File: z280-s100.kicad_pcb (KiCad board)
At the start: 4 copper layers, 254 x 134.6 mm, 58 parts, among them J10 Config (3x8), J7 Serial (2x5), J8 S-100 edge, J9 JTAG (1x6), U1 Z280 (PLCC-68), U10 28C256 even, U11 28C256 odd, U12 7805, U13 DS1813 reset, U14 MAX232, U15 74HCT245 addr0, U16 74HCT245 addr1, U17 74HCT245 addr2, U18 74HCT245 status, U19 74HCT245 control, U2 74HC573 latch, U20 74HCT245 pHLDA, U21 74HCT244 BTI, U22 74F138 decode, U23 74F521 flash win, U24 74F521 slave win, U25 74F245 DO, U26 74F245 DI, U3 74HC573 latch, U4 ATF1508 control, U5 ATF1508 data, U6 SRAM bank0 even, U7 SRAM bank0 odd, U8 SRAM bank1 even, U9 SRAM bank1 odd, Y1 24 MHz crystal

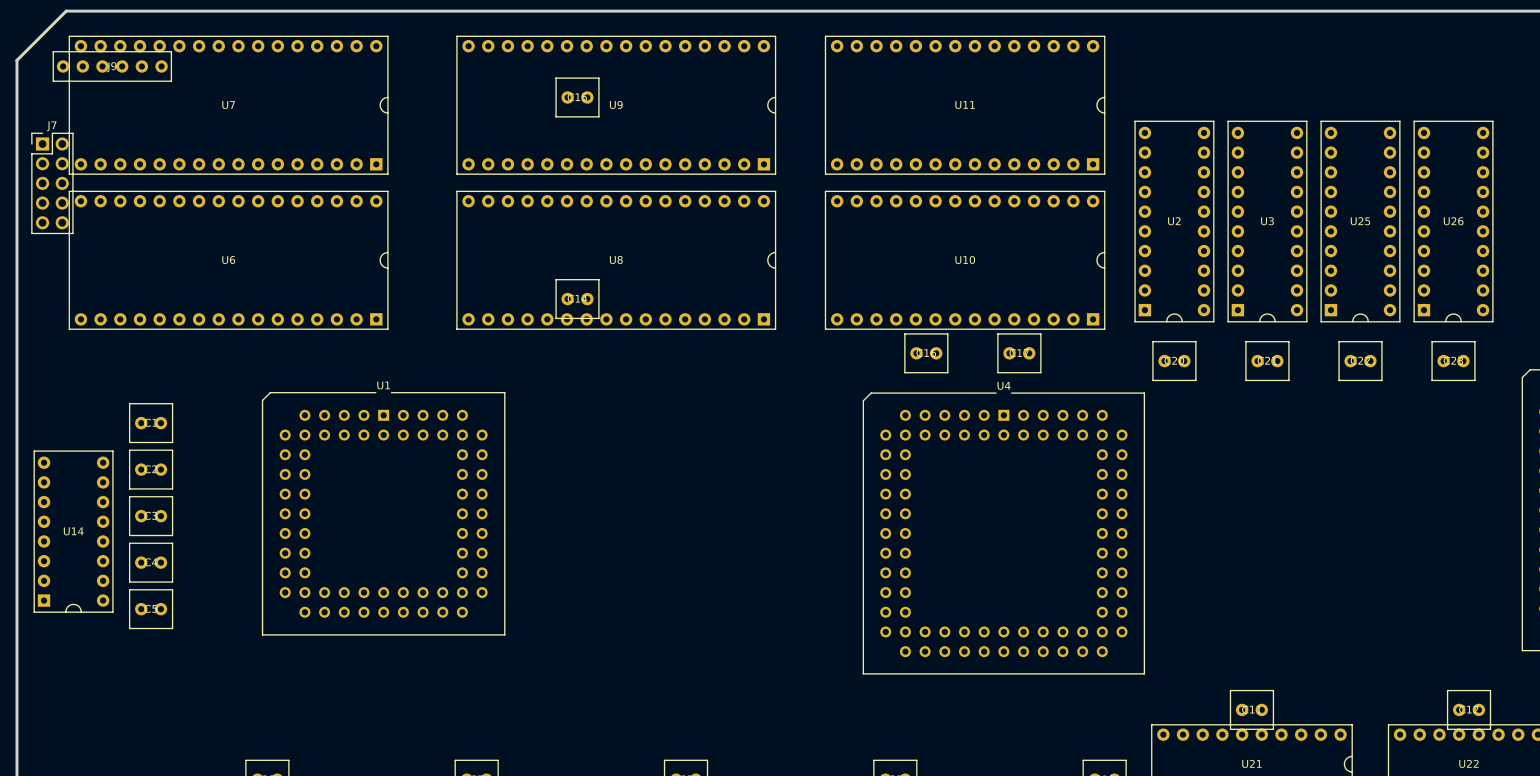
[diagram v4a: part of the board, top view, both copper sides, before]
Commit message: Z280 S-100: fix schematic annotations; rework schematic + PCB placement
The schematic was showing every reference as anonymous (U?, Y?) in KiCad.
Root cause: the symbol instances-block `path` was a filesystem path instead
of the root-sheet UUID, so KiCad couldn't resolve per-instance references.
Also `fields_autoplaced` was "no" (KiCad 9 wants "yes") and the
`sheet_instances` block was missing. Fixed all three.

Schematic placement: console (MAX232 + serial header) moved to the S-100
connector column; U25/U26 data-bus buffers given vertical spacing; U3 moved
down; J10 config and U21 BTI driver moved to the CPU column (x=88).

PCB placement: MAX232 + serial moved under the S-100 connector; data-bus
buffers stacked vertically; address-latch 74HC573s and bypass caps shifted to
match. DRC remains clean (no electrical shorts).

Co-Authored-By: Claude Code <noreply@anthropic.com>
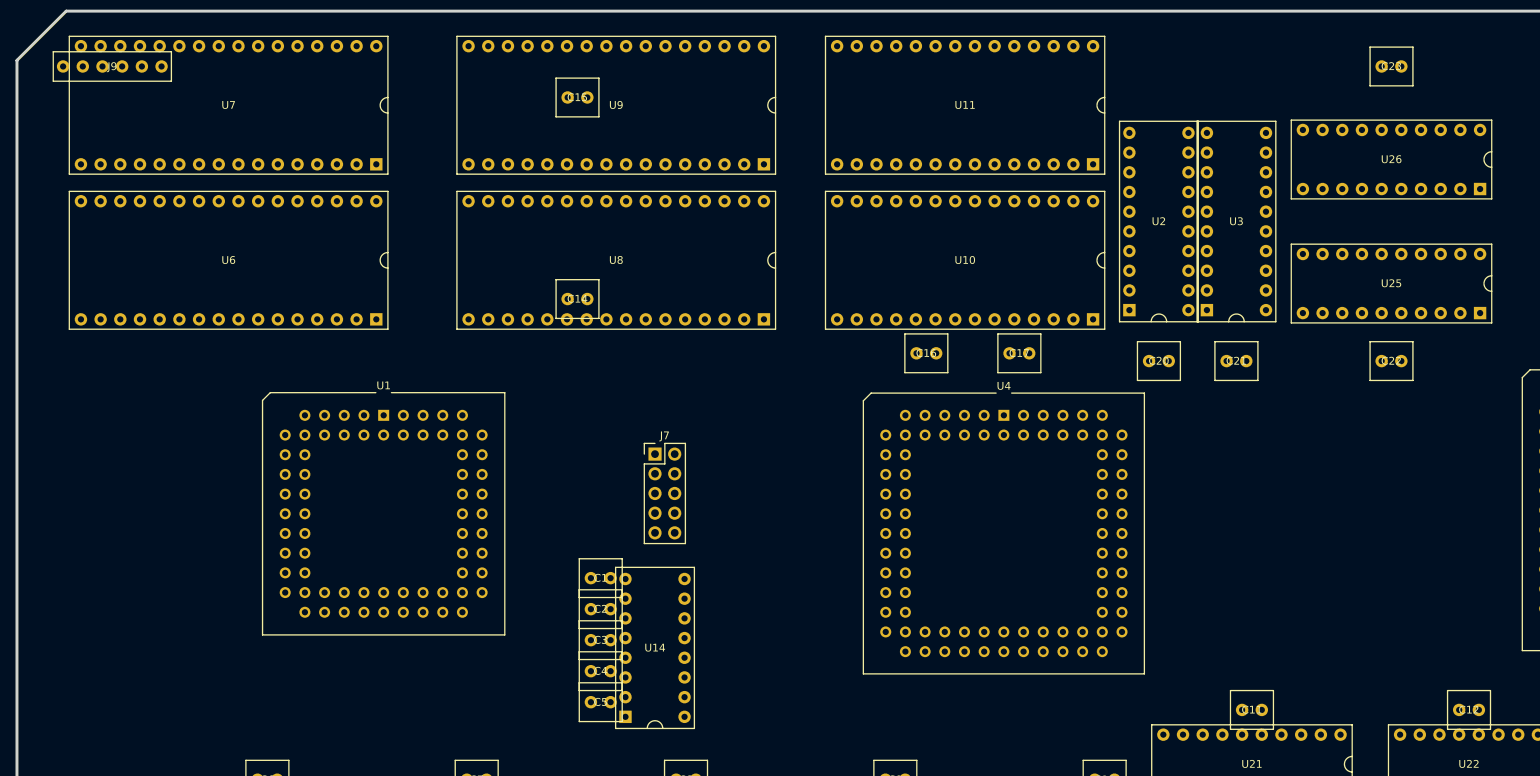
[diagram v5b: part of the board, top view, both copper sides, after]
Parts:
- moved J7 88.5 mm to (95.0, 80.0)
- moved U14 76.5 mm to (95.0, 105.0)
- moved C1 61.4 mm to (88.0, 96.0)
- moved C2 60.7 mm to (88.0, 100.0)
- moved C3 60.2 mm to (88.0, 104.0)
- moved C4 59.7 mm to (88.0, 108.0)
- moved C5 59.2 mm to (88.0, 112.0)
- moved C23 38.8 mm to (190.0, 30.0)
- moved U26 11.3 mm to (190.0, 42.0), turned to 90 degrees
- moved U25 8.94 mm to (190.0, 58.0), turned to 90 degrees
- moved C21 4.00 mm to (170.0, 68.0)
- moved C22 4.00 mm to (190.0, 68.0)
- moved U3 4.00 mm to (170.0, 50.0)
- moved C20 2.00 mm to (160.0, 68.0)
- moved U2 2.00 mm to (160.0, 50.0)
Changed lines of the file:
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@@
   )
   (footprint "DIP-20" (layer "F.Cu")
-    (at 186.0000 50.0000 0)
+    (at 190.0000 58.0000 90)
     (property "Reference" "U25" (at 0 0 0) (layer "F.SilkS")
       (effects (font (size 1 1))))
@@
   )
   (footprint "DIP-20" (layer "F.Cu")
-    (at 198.0000 50.0000 0)
+    (at 190.0000 42.0000 90)
     (property "Reference" "U26" (at 0 0 0) (layer "F.SilkS")
       (effects (font (size 1 1))))
@@
   )
   (footprint "DIP-20" (layer "F.Cu")
-    (at 162.0000 50.0000 0)
+    (at 160.0000 50.0000 0)
     (property "Reference" "U2" (at 0 0 0) (layer "F.SilkS")
       (effects (font (size 1 1))))
@@
   )
   (footprint "DIP-20" (layer "F.Cu")
-    (at 174.0000 50.0000 0)
+    (at 170.0000 50.0000 0)
     (property "Reference" "U3" (at 0 0 0) (layer "F.SilkS")
       (effects (font (size 1 1))))
@@
   )
   (footprint "DIP-16" (layer "F.Cu")
-    (at 20.0000 90.0000 0)
+    (at 95.0000 105.0000 0)
     (property "Reference" "U14" (at 0 0 0) (layer "F.SilkS")
       (effects (font (size 1 1))))
@@
 (footprint "Connector_PinHeader_2.54mm:PinHeader_2x05_P2.54mm_Vertical"
 	(layer "F.Cu")
-  (at 16.0000 40.0000 0)
+  (at 95.0000 80.0000 0)
 	(property "Reference" "J7"
 		(at 1.27 -2.38 0)
@@
   )
   (footprint "CAP-2" (layer "F.Cu")
-    (at 30.0000 76.0000 0)
+    (at 88.0000 96.0000 0)
     (property "Reference" "C1" (at 0 0 0) (layer "F.SilkS")
       (effects (font (size 1 1))))
@@
   )
   (footprint "CAP-2" (layer "F.Cu")
-    (at 30.0000 82.0000 0)
+    (at 88.0000 100.0000 0)
     (property "Reference" "C2" (at 0 0 0) (layer "F.SilkS")
       (effects (font (size 1 1))))
@@
   )
   (footprint "CAP-2" (layer "F.Cu")
-    (at 30.0000 88.0000 0)
+    (at 88.0000 104.0000 0)
     (property "Reference" "C3" (at 0 0 0) (layer "F.SilkS")
       (effects (font (size 1 1))))
@@
   )
   (footprint "CAP-2" (layer "F.Cu")
-    (at 30.0000 94.0000 0)
+    (at 88.0000 108.0000 0)
     (property "Reference" "C4" (at 0 0 0) (layer "F.SilkS")
       (effects (font (size 1 1))))
@@
   )
   (footprint "CAP-2" (layer "F.Cu")
-    (at 30.0000 100.0000 0)
+    (at 88.0000 112.0000 0)
     (property "Reference" "C5" (at 0 0 0) (layer "F.SilkS")
       (effects (font (size 1 1))))
@@
   )
   (footprint "CAP-2" (layer "F.Cu")
-    (at 162.0000 68.0000 0)
+    (at 160.0000 68.0000 0)
     (property "Reference" "C20" (at 0 0 0) (layer "F.SilkS")
       (effects (font (size 1 1))))
@@
   )
   (footprint "CAP-2" (layer "F.Cu")
-    (at 174.0000 68.0000 0)
+    (at 170.0000 68.0000 0)
     (property "Reference" "C21" (at 0 0 0) (layer "F.SilkS")
       (effects (font (size 1 1))))
@@
   )
   (footprint "CAP-2" (layer "F.Cu")
-    (at 186.0000 68.0000 0)
+    (at 190.0000 68.0000 0)
     (property "Reference" "C22" (at 0 0 0) (layer "F.SilkS")
       (effects (font (size 1 1))))
@@
   )
   (footprint "CAP-2" (layer "F.Cu")
-    (at 198.0000 68.0000 0)
+    (at 190.0000 30.0000 0)
     (property "Reference" "C23" (at 0 0 0) (layer "F.SilkS")
       (effects (font (size 1 1))))

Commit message: Z280 S-100: deterministic schematic UUIDs; unify S-100 footprint name
uid() now derives each schematic UUID from a stable identity key (uuid5) instead of uuid4, so regenerating the schematic no longer churns symbol UUIDs; the board's footprint (path ...) links survive Update PCB from Schematic.

S-100 edge connector footprint unified on S100_MALE (the schematic carried a phantom Connector_Edge that broke net updates). Sync U27/Y2/U13/J7 positions from the schematic; regenerate the netlist and update the board's 42 footprint path UUIDs to match.

Also rename decode signal BANK -> A20 and convert DIP/header placements to library footprints in gen_pcb.py.

Co-Authored-By: Claude Code <noreply@anthropic.com>
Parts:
- added U27: LM323K, Package_TO_SOT_THT:TO-3, F.Cu at (50.5, 123.2)
- added Y2: 24 MHz, z280-s100:Oscillator_DIP-8-14, F.Cu at (85.9, 96.0)
- C1, C2, C3, C4, C5: footprint CAP-2 -> Capacitor_THT:C_Disc_D5.0mm_W2.5mm_P2.50mm
- C14, C15: moved to B.Cu
- J10: value Config (3x8) -> Config header (3x8)
- J7: value Serial (2x5) -> Serial header (2x5)
- J8: value S-100 edge -> S-100 edge connector (100-pin)
- J9: value JTAG (1x6) -> JTAG header (1x6); footprint HDR-6 -> Connector_PinHeader_2.54mm:PinHeader_1x06_P2.54mm_Vertical
- R1: value 1k pRDY -> 1k; footprint HDR-2 -> Resistor_THT:R_Axial_DIN0207_L6.3mm_D2.5mm_P7.62mm_Horizontal
- R2: value 1k XRDY -> 1k; footprint HDR-2 -> Resistor_THT:R_Axial_DIN0207_L6.3mm_D2.5mm_P7.62mm_Horizontal
- R3: value 1k SLAVE_ONLY -> 1k; footprint HDR-2 -> Resistor_THT:R_Axial_DIN0207_L6.3mm_D2.5mm_P7.62mm_Horizontal
- R4: value 1k SIXTN -> 1k; footprint HDR-2 -> Resistor_THT:R_Axial_DIN0207_L6.3mm_D2.5mm_P7.62mm_Horizontal
- U1: value Z280 (PLCC-68) -> Z280 Z-BUS (12 MHz)
- U10: value 28C256 even -> AT28C256 (32Kx8); footprint DIP-28 -> Package_DIP:DIP-28_W15.24mm
- U11: value 28C256 odd -> AT28C256 (32Kx8); footprint DIP-28 -> Package_DIP:DIP-28_W15.24mm
- U12: value 7805 -> LM7805; footprint HDR-3 -> Package_TO_SOT_THT:TO-220-3_Horizontal_TabDown
- U13: value DS1813 reset -> DS1813; footprint HDR-3 -> Package_TO_SOT_THT:TO-92_Inline
- U14: footprint DIP-16 -> Package_DIP:DIP-16_W7.62mm
- U15: value 74HCT245 addr0 -> 74HCT245; footprint DIP-20 -> Package_DIP:DIP-20_W7.62mm
- U16: value 74HCT245 addr1 -> 74HCT245; footprint DIP-20 -> Package_DIP:DIP-20_W7.62mm
- U17: value 74HCT245 addr2 -> 74HCT245; footprint DIP-20 -> Package_DIP:DIP-20_W7.62mm
- U18: value 74HCT245 status -> 74HCT245; footprint DIP-20 -> Package_DIP:DIP-20_W7.62mm
- U19: value 74HCT245 control -> 74HCT245; footprint DIP-20 -> Package_DIP:DIP-20_W7.62mm
- U2, U3: value 74HC573 latch -> 74HC573; footprint DIP-20 -> Package_DIP:DIP-20_W7.62mm
- U20: value 74HCT245 pHLDA -> 74HCT245; footprint DIP-20 -> Package_DIP:DIP-20_W7.62mm
- U21: value 74HCT244 BTI -> 74HCT244; footprint DIP-20 -> Package_DIP:DIP-20_W7.62mm
- U22: value 74F138 decode -> 74F138; footprint DIP-16 -> Package_DIP:DIP-16_W7.62mm
- U23: value 74F521 flash win -> 74F521; footprint DIP-20 -> Package_DIP:DIP-20_W7.62mm
- U24: value 74F521 slave win -> 74F521; footprint DIP-20 -> Package_DIP:DIP-20_W7.62mm
- U25: value 74F245 DO -> 74F245; footprint DIP-20 -> Package_DIP:DIP-20_W7.62mm
- U26: value 74F245 DI -> 74F245; footprint DIP-20 -> Package_DIP:DIP-20_W7.62mm
- U4: value ATF1508 control -> ATF1508AS (PLCC-84)
- U5: value ATF1508 data -> ATF1508AS (PLCC-84)
- U6: value SRAM bank0 even -> IS61C5128AS-25QLI (512Kx8); footprint DIP-32 -> Package_DIP:DIP-32_W15.24mm
- U7: value SRAM bank0 odd -> IS61C5128AS-25QLI (512Kx8); footprint DIP-32 -> Package_DIP:DIP-32_W15.24mm
- U8: value SRAM bank1 even -> IS61C5128AS-25QLI (512Kx8); footprint DIP-32 -> Package_DIP:DIP-32_W15.24mm
- U9: value SRAM bank1 odd -> IS61C5128AS-25QLI (512Kx8); footprint DIP-32 -> Package_DIP:DIP-32_W15.24mm
- Y1: value 24 MHz crystal -> 24 MHz
- moved J9 240.2 mm to (256.3, 95.0), turned to -90 degrees
- moved U12 237.3 mm to (20.6, 142.6)
- moved J10 199.5 mm to (21.3, 76.2)
- moved C1 161.3 mm to (234.7, 28.8)
- moved C2 161.3 mm to (234.7, 32.8)
- moved C3 161.3 mm to (234.7, 36.8)
- moved C4 161.3 mm to (234.7, 40.8)
- moved C5 161.3 mm to (234.7, 44.8)
- moved R4 157.2 mm to (109.0, 95.2)
- moved U24 155.8 mm to (96.3, 114.6), turned to 0 degrees
- moved Y1 155.8 mm to (96.5, 79.8)
- moved U21 155.4 mm to (21.1, 83.1), turned to 0 degrees
- moved R2 148.7 mm to (108.7, 89.7)
- moved U23 146.6 mm to (79.5, 114.6), turned to 0 degrees
- moved R1 145.1 mm to (109.0, 84.3)
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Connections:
- C3 pad 2: GND -> +5V
- C4 pad 2: GND -> +5V
- C5 pad 2: GND -> +5V
- J10 pad 12: GND -> +5V
- J10 pad 15: GND -> +5V
- J10 pad 18: GND -> +5V
- J10 pad 21: GND -> +5V
- J10 pad 24: GND -> +5V
- J10 pad 3: GND -> +5V
- J10 pad 6: GND -> +5V
- J10 pad 9: GND -> +5V
- J7 pad 10: GND -> +5V
- J7 pad 3: GND -> +5V
- J7 pad 4: GND -> +5V
- J7 pad 5: GND -> +5V
- J7 pad 6: GND -> +5V
- J7 pad 7: GND -> +5V
- J7 pad 8: GND -> +5V
- J7 pad 9: GND -> +5V
- J8 pad 21: (no net) -> unconnected-(J8-NC-Pad21)
- J8 pad 27: (no net) -> unconnected-(J8-NC-Pad27)
- J8 pad 28: (no net) -> unconnected-(J8-NC-Pad28)
- J8 pad 65: (no net) -> unconnected-(J8-NC-Pad65)
- J8 pad 66: (no net) -> unconnected-(J8-NC-Pad66)
- J8 pad 69: (no net) -> unconnected-(J8-NC-Pad69)
- J8 pad 71: (no net) -> unconnected-(J8-NC-Pad71)
- J9 pad 5: GND -> +5V
- R3 pad 1: GND -> +5V
- U1 pad 1: GND -> +5V
- U1 pad 11: (no net) -> unconnected-(U1-DMASTB0-Pad11)
- U1 pad 13: (no net) -> unconnected-(U1-DMASTB1-Pad13)
- U1 pad 20: (no net) -> unconnected-(U1-CTIO1-Pad20)
- U1 pad 23: (no net) -> unconnected-(U1-CTIO2-Pad23)
- U1 pad 25: (no net) -> unconnected-(U1-CTIN2-Pad25)
- U1 pad 26: (no net) -> unconnected-(U1-INT-C-Pad26)
- U1 pad 30: (no net) -> unconnected-(U1-CTIO0/GREQ-Pad30)
- U1 pad 32: (no net) -> unconnected-(U1-CTIN0/GACK-Pad32)
- U1 pad 33: (no net) -> unconnected-(U1-PAUSE-Pad33)
- U1 pad 35: GND -> +5V
- U1 pad 36: (no net) -> unconnected-(U1-INT-B/EOP-B-Pad36)
- U1 pad 41: (no net) -> unconnected-(U1-CTIN1-Pad41)
- U1 pad 50: XTALI -> +5V
- U1 pad 51: GND -> +5V
- U1 pad 52: (no net) -> unconnected-(U1-RESERVED-Pad52)
- U1 pad 53: GND -> +5V
- U1 pad 55: (no net) -> unconnected-(U1-RDY0-Pad55)
- U1 pad 56: (no net) -> unconnected-(U1-RDY1-Pad56)
- U1 pad 58: (no net) -> unconnected-(U1-RDY3-Pad58)
- U1 pad 63: (no net) -> unconnected-(U1-RDY2-Pad63)
- U10 pad 14: GND -> +5V
- U11 pad 14: GND -> +5V
- U13 pad 1: GND -> +5V
- U14 pad 15: GND -> +5V
- U15 pad 10: GND -> +5V
- U16 pad 10: GND -> +5V
- U17 pad 10: GND -> +5V
- U18 pad 10: GND -> +5V
- U18 pad 18: (no net) -> unconnected-(U18-B7-Pad18)
- U18 pad 9: (no net) -> unconnected-(U18-A7-Pad9)
- U19 pad 10: GND -> +5V
- U19 pad 15: (no net) -> unconnected-(U19-B4-Pad15)
- U19 pad 16: (no net) -> unconnected-(U19-B5-Pad16)
- U19 pad 17: (no net) -> unconnected-(U19-B6-Pad17)
- U19 pad 18: (no net) -> unconnected-(U19-B7-Pad18)
- U19 pad 6: (no net) -> unconnected-(U19-A4-Pad6)
- U19 pad 7: (no net) -> unconnected-(U19-A5-Pad7)
- U19 pad 8: (no net) -> unconnected-(U19-A6-Pad8)
- U19 pad 9: (no net) -> unconnected-(U19-A7-Pad9)
- U2 pad 10: GND -> +5V
- U20 pad 10: GND -> +5V
- U20 pad 12: (no net) -> unconnected-(U20-B1-Pad12)
- U20 pad 13: (no net) -> unconnected-(U20-B2-Pad13)
- U20 pad 14: (no net) -> unconnected-(U20-B3-Pad14)
- U20 pad 15: (no net) -> unconnected-(U20-B4-Pad15)
- U20 pad 16: (no net) -> unconnected-(U20-B5-Pad16)
- U20 pad 17: (no net) -> unconnected-(U20-B6-Pad17)
- U20 pad 18: (no net) -> unconnected-(U20-B7-Pad18)
- U20 pad 19: GND -> +5V
- U20 pad 3: GND -> +5V
- U20 pad 4: GND -> +5V
- U20 pad 5: GND -> +5V
- U20 pad 6: GND -> +5V
- U20 pad 7: GND -> +5V
- U20 pad 8: GND -> +5V
- U20 pad 9: GND -> +5V
- U21 pad 10: GND -> +5V
- U22 pad 10: (no net) -> unconnected-(U22-Y5-Pad10)
- U22 pad 11: (no net) -> unconnected-(U22-Y4-Pad11)
- U22 pad 12: (no net) -> unconnected-(U22-Y3-Pad12)
- U22 pad 13: (no net) -> unconnected-(U22-Y2-Pad13)
- U22 pad 14: (no net) -> unconnected-(U22-Y1-Pad14)
- U22 pad 4: GND -> +5V
- U22 pad 5: GND -> +5V
- U22 pad 7: (no net) -> unconnected-(U22-Y7-Pad7)
- U22 pad 8: GND -> +5V
- U22 pad 9: (no net) -> unconnected-(U22-Y6-Pad9)
- U23 pad 1: GND -> +5V
- U23 pad 10: GND -> +5V
- U23 pad 2: GND -> +5V
- U23 pad 4: GND -> +5V
- U23 pad 6: GND -> +5V
- U23 pad 8: GND -> +5V
- U24 pad 1: GND -> +5V
- U24 pad 10: GND -> +5V
- U24 pad 14: GND -> +5V
- U24 pad 16: GND -> +5V
- U24 pad 18: GND -> +5V
- U25 pad 10: GND -> +5V
- U25 pad 19: GND -> +5V
- U26 pad 10: GND -> +5V
- U26 pad 19: GND -> +5V
- U3 pad 10: GND -> +5V
- U3 pad 17: (no net) -> unconnected-(U3-Q5-Pad17)
- U3 pad 18: (no net) -> unconnected-(U3-Q6-Pad18)
- U3 pad 19: (no net) -> unconnected-(U3-Q7-Pad19)
- U3 pad 7: GND -> +5V
- U3 pad 8: GND -> +5V
- U3 pad 9: GND -> +5V
- U4 pad 19: GND -> +5V
- U4 pad 32: GND -> +5V
- U4 pad 33: BANK -> A20
- U4 pad 42: GND -> +5V
- U4 pad 47: GND -> +5V
- U4 pad 59: GND -> +5V
- U4 pad 7: GND -> +5V
- U4 pad 72: GND -> +5V
- U4 pad 82: GND -> +5V
- U5 pad 19: GND -> +5V
- U5 pad 32: GND -> +5V
- U5 pad 42: GND -> +5V
- U5 pad 47: GND -> +5V
- U5 pad 59: GND -> unconnected-(U5-GND-Pad59)
- U5 pad 7: GND -> +5V
- U5 pad 72: GND -> +5V
- U5 pad 82: GND -> +5V
- U6 pad 1: A15 -> A18
- U6 pad 10: A1 -> A3
- U6 pad 11: AD8 -> A2
- U6 pad 12: AD9 -> A1
- U6 pad 13: AD10 -> AD8
- U6 pad 14: GND -> AD9
- U6 pad 15: AD11 -> AD10
- U6 pad 16: AD12 -> +5V
- U6 pad 17: AD13 -> AD11
- U6 pad 18: AD14 -> AD12
- U6 pad 19: AD15 -> AD13
- U6 pad 2: A13 -> A17
- U6 pad 20: MEM_CE0 -> AD14
- U6 pad 21: A11 -> AD15
- U6 pad 22: MEM_OE -> MEM_CE0
- U6 pad 23: A12 -> A11
- U6 pad 24: A10 -> MEM_OE
- U6 pad 25: A9 -> A12
- U6 pad 26: A14 -> A10
- U6 pad 27: MEM_WE_L -> A9
- U6 pad 28: +5V -> A14
- U6 pad 29: A19 -> MEM_WE_L
- U6 pad 3: A8 -> A15
- U6 pad 30: A18 -> A19
- U6 pad 31: A17 -> A16
- U6 pad 32: A16 -> +5V
- U6 pad 4: A7 -> A13
- U6 pad 5: A6 -> A8
- U6 pad 6: A5 -> A7
- U6 pad 7: A4 -> A6
- U6 pad 8: A3 -> A5
- U6 pad 9: A2 -> A4
- U7 pad 1: A15 -> A18
- U7 pad 10: A1 -> A3
- U7 pad 11: AD0 -> A2
- U7 pad 12: AD1 -> A1
- U7 pad 13: AD2 -> AD0
- U7 pad 14: GND -> AD1
- U7 pad 15: AD3 -> AD2
- U7 pad 16: AD4 -> +5V
- U7 pad 17: AD5 -> AD3
- U7 pad 18: AD6 -> AD4
- U7 pad 19: AD7 -> AD5
- U7 pad 2: A13 -> A17
- U7 pad 20: MEM_CE0 -> AD6
- U7 pad 21: A11 -> AD7
- U7 pad 22: MEM_OE -> MEM_CE0
- U7 pad 23: A12 -> A11
- U7 pad 24: A10 -> MEM_OE
- U7 pad 25: A9 -> A12
- U7 pad 26: A14 -> A10
- U7 pad 27: MEM_WE_H -> A9
- U7 pad 28: +5V -> A14
- U7 pad 29: A19 -> MEM_WE_H
- U7 pad 3: A8 -> A15
- U7 pad 30: A18 -> A19
- U7 pad 31: A17 -> A16
- U7 pad 32: A16 -> +5V
- U7 pad 4: A7 -> A13
- U7 pad 5: A6 -> A8
- U7 pad 6: A5 -> A7
- U7 pad 7: A4 -> A6
- U7 pad 8: A3 -> A5
- U7 pad 9: A2 -> A4
- U8 pad 1: A15 -> A18
- U8 pad 10: A1 -> A3
- U8 pad 11: AD8 -> A2
- U8 pad 12: AD9 -> A1
- U8 pad 13: AD10 -> AD8
- U8 pad 14: GND -> AD9
- U8 pad 15: AD11 -> AD10
- U8 pad 16: AD12 -> +5V
- U8 pad 17: AD13 -> AD11
- U8 pad 18: AD14 -> AD12
- U8 pad 19: AD15 -> AD13
- U8 pad 2: A13 -> A17
- U8 pad 20: MEM_CE1 -> AD14
- U8 pad 21: A11 -> AD15
- U8 pad 22: MEM_OE -> MEM_CE1
- U8 pad 23: A12 -> A11
- U8 pad 24: A10 -> MEM_OE
- U8 pad 25: A9 -> A12
- U8 pad 26: A14 -> A10
- U8 pad 27: MEM_WE_L -> A9
- U8 pad 28: +5V -> A14
- U8 pad 29: A19 -> MEM_WE_L
- U8 pad 3: A8 -> A15
- U8 pad 30: A18 -> A19
- U8 pad 31: A17 -> A16
- U8 pad 32: A16 -> +5V
- U8 pad 4: A7 -> A13
- U8 pad 5: A6 -> A8
- U8 pad 6: A5 -> A7
- U8 pad 7: A4 -> A6
- U8 pad 8: A3 -> A5
- U8 pad 9: A2 -> A4
- U9 pad 1: A15 -> A18
- U9 pad 10: A1 -> A3
- U9 pad 11: AD0 -> A2
- U9 pad 12: AD1 -> A1
- U9 pad 13: AD2 -> AD0
- U9 pad 14: GND -> AD1
- U9 pad 15: AD3 -> AD2
- U9 pad 16: AD4 -> +5V
- U9 pad 17: AD5 -> AD3
- U9 pad 18: AD6 -> AD4
- U9 pad 19: AD7 -> AD5
- U9 pad 2: A13 -> A17
- U9 pad 20: MEM_CE1 -> AD6
- U9 pad 21: A11 -> AD7
- U9 pad 22: MEM_OE -> MEM_CE1
- U9 pad 23: A12 -> A11
- U9 pad 24: A10 -> MEM_OE
- U9 pad 25: A9 -> A12
- U9 pad 26: A14 -> A10
- U9 pad 27: MEM_WE_H -> A9
- U9 pad 28: +5V -> A14
- U9 pad 29: A19 -> MEM_WE_H
- U9 pad 3: A8 -> A15
- U9 pad 30: A18 -> A19
- U9 pad 31: A17 -> A16
- U9 pad 32: A16 -> +5V
- U9 pad 4: A7 -> A13
- U9 pad 5: A6 -> A8
- U9 pad 6: A5 -> A7
- U9 pad 7: A4 -> A6
- U9 pad 8: A3 -> A5
- U9 pad 9: A2 -> A4
- Y1 pad 1: XTALI -> +5V
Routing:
- net GND: track 0.00 -> 105.6 mm, vias 1 -> 4
- net +8V: track 0.00 -> 73.1 mm
- net S100_pDBIN: track 0.00 -> 6.44 mm
- net S100_ERROR: track 0.00 -> 6.44 mm
- net S100_DO2: track 0.00 -> 6.44 mm
- net S100_DI6: track 0.00 -> 6.44 mm
- net S100_A7: track 0.00 -> 6.44 mm
- net unconnected-(J8-NC-Pad71): track 0.00 -> 6.44 mm, vias 0 -> 1
- net unconnected-(J8-NC-Pad66): track 0.00 -> 6.44 mm, vias 0 -> 1
- net unconnected-(J8-NC-Pad65): track 0.00 -> 6.44 mm, vias 0 -> 1
- net S100_SIXTN: track 0.00 -> 6.44 mm
- net S100_DMA1: track 0.00 -> 6.44 mm
- net S100_DMA0: track 0.00 -> 6.44 mm
- net S100_A20: track 0.00 -> 6.44 mm
- net -16V: track 0.00 -> 6.44 mm
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- added copper zone on B.Cu, net +5V
- removed copper zone on In2.Cu, net +5V
- removed copper zone on In1.Cu, net GND

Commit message: Z280 S-100: clean 2+2 stackup — GND/+5V planes, +8V island, ready to route
- GND plane on In1.Cu, +5V plane on In2.Cu (through-hole thermal relief)
- +8V copper island on In2.Cu (bottom-left) feeding the two regulators
- 18 decoupling caps placed on-board; memory chips U6-U11 spread to 24 mm pitch
- test-point finger->via traces restored from hand layout; signal routing cleared to a clean slate
- gen_pcb.py positions synced to the hand-tweaked placement

Co-Authored-By: Claude Code <noreply@anthropic.com>
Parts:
- J8: value S-100 edge connector (100-pin) -> S-100
- U1: value Z280 Z-BUS (12 MHz) -> Z280 Z-BUS
- U10: value AT28C256 (32Kx8) -> AT28C256 HI
- U11: value AT28C256 (32Kx8) -> AT28C256 LO
- U6: value IS61C5128AS-25QLI (512Kx8) -> RAM0 HI
- U7: value IS61C5128AS-25QLI (512Kx8) -> RAM0 LO
- U8: value IS61C5128AS-25QLI (512Kx8) -> RAM1 HI
- U9: value IS61C5128AS-25QLI (512Kx8) -> RAM1 LO
- moved C19 187.1 mm to (55.2, 96.1)
- moved C17 163.1 mm to (162.8, 109.0), turned to 180 degrees
- moved C20 124.5 mm to (69.0, 116.3)
- moved C10 109.7 mm to (95.3, 40.0)
- moved U2 106.6 mm to (50.5, 42.8)
- moved U3 105.8 mm to (62.9, 42.8)
- moved C21 105.3 mm to (106.9, 114.2)
- moved C11 103.9 mm to (119.3, 40.0)
- moved C16 101.5 mm to (112.0, 92.0)
- moved C13 99.9 mm to (179.1, 27.1)
- moved C12 97.5 mm to (143.3, 40.0)
- moved C14 90.9 mm to (202.8, 27.1)
- moved R2 87.6 mm to (21.2, 86.4)
- moved R1 87.6 mm to (21.5, 81.0)
- moved R4 87.6 mm to (21.5, 91.9)
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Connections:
- C3 pad 2: +5V -> GND
- C4 pad 2: +5V -> GND
- C5 pad 2: +5V -> GND
- J10 pad 12: +5V -> GND
- J10 pad 15: +5V -> GND
- J10 pad 18: +5V -> GND
- J10 pad 21: +5V -> GND
- J10 pad 24: +5V -> GND
- J10 pad 3: +5V -> GND
- J10 pad 6: +5V -> GND
- J10 pad 9: +5V -> GND
- J7 pad 10: +5V -> GND
- J7 pad 3: +5V -> GND
- J7 pad 4: +5V -> GND
- J7 pad 5: +5V -> GND
- J7 pad 6: +5V -> GND
- J7 pad 7: +5V -> GND
- J7 pad 8: +5V -> GND
- J7 pad 9: +5V -> GND
- J9 pad 5: +5V -> GND
- R3 pad 1: +5V -> GND
- U1 pad 1: +5V -> GND
- U1 pad 35: +5V -> GND
- U1 pad 50: +5V -> XTALI
- U1 pad 51: +5V -> GND
- U1 pad 53: +5V -> GND
- U10 pad 14: +5V -> GND
- U11 pad 14: +5V -> GND
- U13 pad 1: +5V -> GND
- U14 pad 15: +5V -> GND
- U15 pad 10: +5V -> GND
- U16 pad 10: +5V -> GND
- U17 pad 10: +5V -> GND
- U18 pad 10: +5V -> GND
- U19 pad 10: +5V -> GND
- U2 pad 10: +5V -> GND
- U20 pad 10: +5V -> GND
- U20 pad 19: +5V -> GND
- U20 pad 3: +5V -> GND
- U20 pad 4: +5V -> GND
- U20 pad 5: +5V -> GND
- U20 pad 6: +5V -> GND
- U20 pad 7: +5V -> GND
- U20 pad 8: +5V -> GND
- U20 pad 9: +5V -> GND
- U21 pad 10: +5V -> GND
- U22 pad 4: +5V -> GND
- U22 pad 5: +5V -> GND
- U22 pad 8: +5V -> GND
- U23 pad 1: +5V -> GND
- U23 pad 10: +5V -> GND
- U23 pad 2: +5V -> GND
- U23 pad 4: +5V -> GND
- U23 pad 6: +5V -> GND
- U23 pad 8: +5V -> GND
- U24 pad 1: +5V -> GND
- U24 pad 10: +5V -> GND
- U24 pad 14: +5V -> GND
- U24 pad 16: +5V -> GND
- U24 pad 18: +5V -> GND
- U25 pad 10: +5V -> GND
- U25 pad 19: +5V -> GND
- U26 pad 10: +5V -> GND
- U26 pad 19: +5V -> GND
- U3 pad 10: +5V -> GND
- U3 pad 7: +5V -> GND
- U3 pad 8: +5V -> GND
- U3 pad 9: +5V -> GND
- U4 pad 19: +5V -> GND
- U4 pad 32: +5V -> GND
- U4 pad 42: +5V -> GND
- U4 pad 47: +5V -> GND
- U4 pad 59: +5V -> GND
- U4 pad 7: +5V -> GND
- U4 pad 72: +5V -> GND
- U4 pad 82: +5V -> GND
- U5 pad 19: +5V -> GND
- U5 pad 32: +5V -> GND
- U5 pad 42: +5V -> GND
- U5 pad 47: +5V -> GND
- U5 pad 59: unconnected-(U5-GND-Pad59) -> GND
- U5 pad 7: +5V -> GND
- U5 pad 72: +5V -> GND
- U5 pad 82: +5V -> GND
- U6 pad 16: +5V -> GND
- U7 pad 16: +5V -> GND
- U8 pad 16: +5V -> GND
- U9 pad 16: +5V -> GND
- Y1 pad 1: +5V -> XTALI
- Y2 pad 4: +5V -> GND
- Y2 pad 5: +5V -> XTALI
- Y2 pad 7: +5V -> GND
- Y2 pad 8: +5V -> XTALI
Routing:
- net GND: track 105.6 -> 39.8 mm, vias 4 -> 3
- net +8V: track 73.1 -> 13.0 mm
- net S100_ERROR: track 6.44 -> 0.00 mm, vias 1 -> 0
- net unconnected-(J8-NC-Pad71): track 6.44 -> 0.00 mm, vias 1 -> 0
- net unconnected-(J8-NC-Pad66): track 6.44 -> 0.00 mm, vias 1 -> 0
- net unconnected-(J8-NC-Pad65): track 6.44 -> 0.00 mm, vias 1 -> 0
- net S100_DMA1: track 6.44 -> 0.00 mm, vias 1 -> 0
- net S100_DMA0: track 6.44 -> 0.00 mm, vias 1 -> 0
- net -16V: track 6.44 -> 0.00 mm, vias 1 -> 0
- net unconnected-(J8-NC-Pad69): track 6.44 -> 0.00 mm, vias 1 -> 0
- net S100_SLAVE_CLR: track 6.44 -> 0.00 mm, vias 1 -> 0
- net S100_POC: track 6.44 -> 0.00 mm, vias 1 -> 0
- net S100_PHANTOM: track 6.44 -> 0.00 mm, vias 1 -> 0
- net S100_MWRT: track 6.44 -> 0.00 mm, vias 1 -> 0
- net S100_DMA2: track 6.44 -> 0.00 mm, vias 1 -> 0
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- added copper zone on In2.Cu, net +5V
- added copper zone on In2.Cu, net +8V
- added copper zone on In1.Cu, net GND
- removed copper zone on B.Cu, net +5V
